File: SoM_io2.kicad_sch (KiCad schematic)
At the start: 1 part, among them J1 Hermaphroditic_Molex_203456-0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

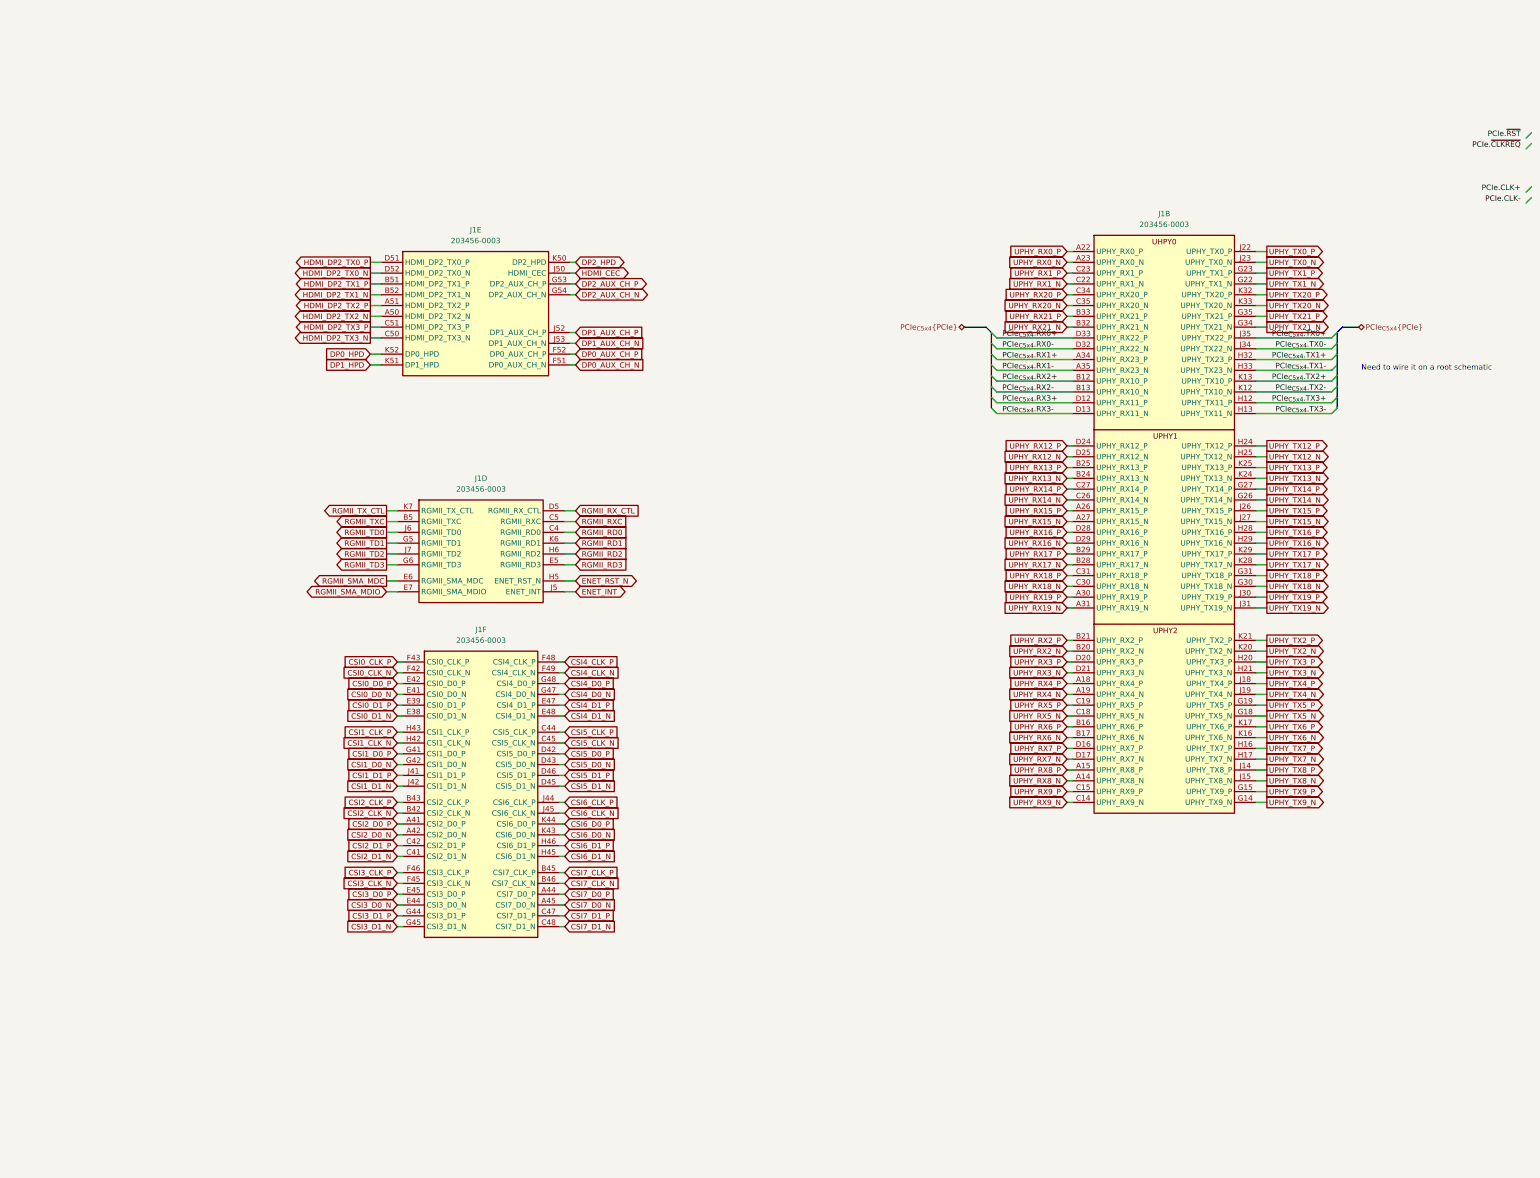
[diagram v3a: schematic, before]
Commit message: [#82048] Continue routing bus connections from M.2 key M to SoM
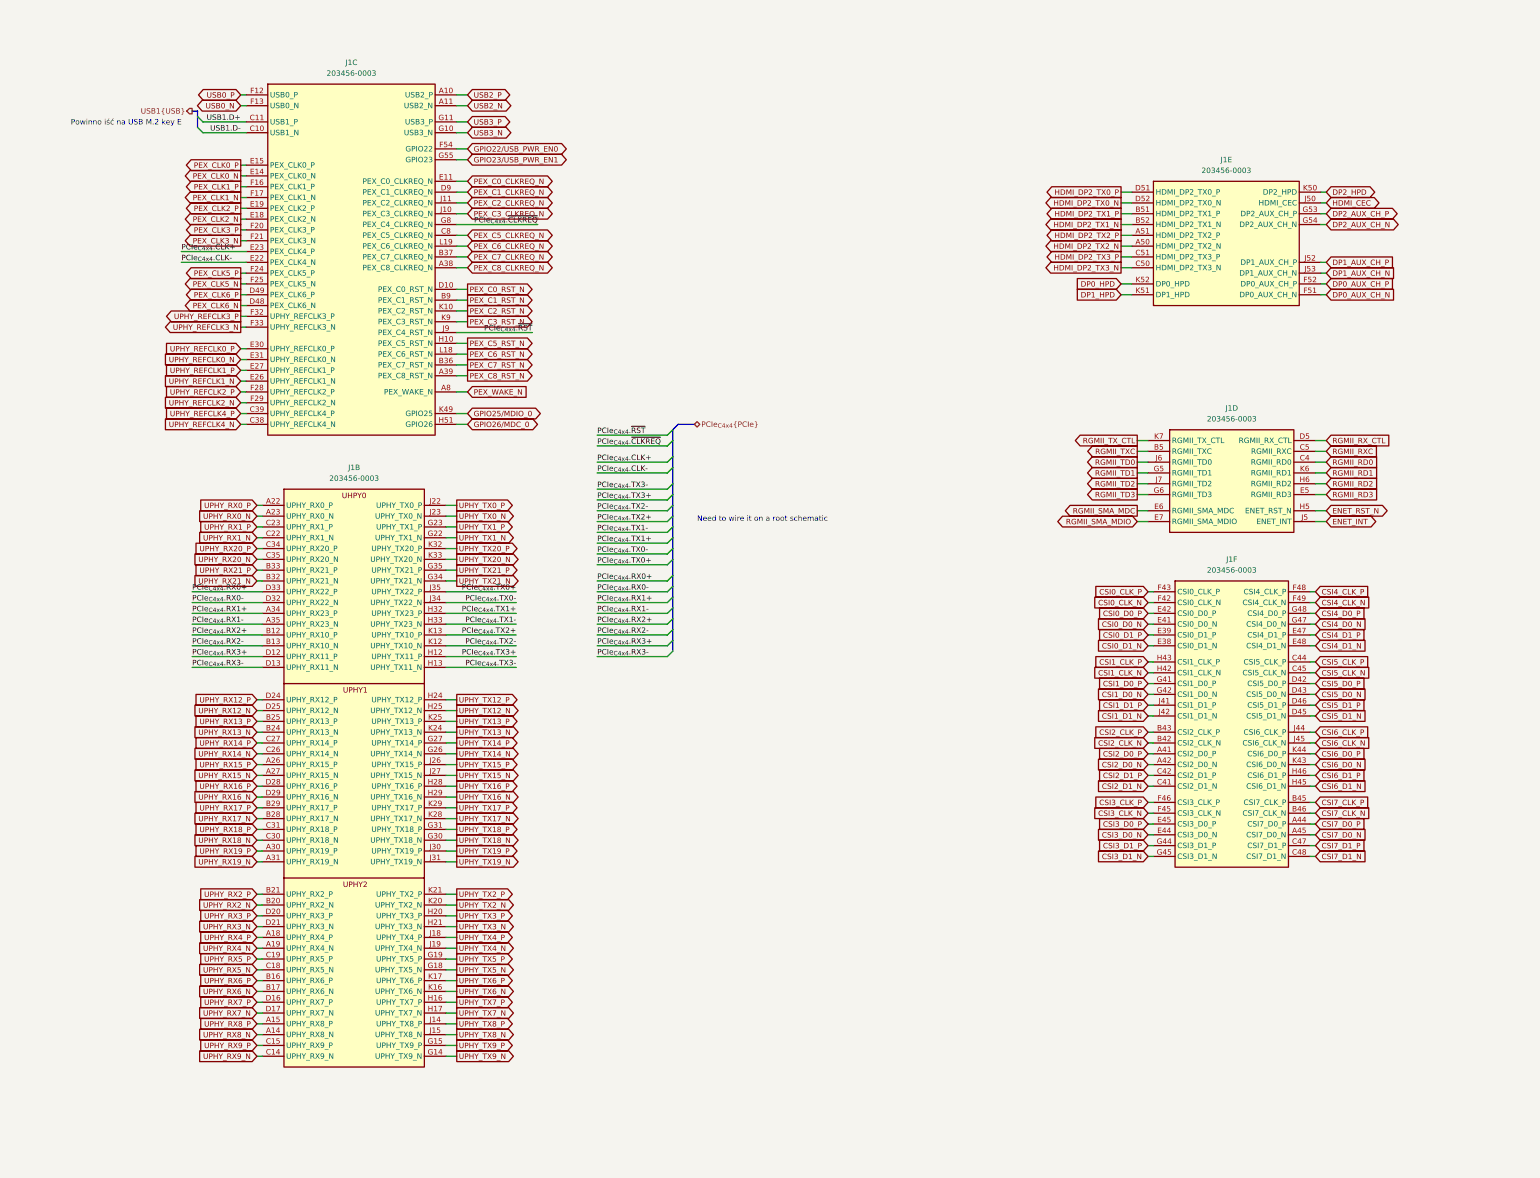
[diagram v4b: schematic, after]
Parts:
- added unit 3 of J1
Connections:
- net PCIe_{C5x4}.RX0+ renamed PCIe_{C4x4}.RX0+
- net PCIe_{C5x4}.RX0- renamed PCIe_{C4x4}.RX0-
- net PCIe_{C5x4}.RX1+ renamed PCIe_{C4x4}.RX1+
- net PCIe_{C5x4}.RX1- renamed PCIe_{C4x4}.RX1-
- net PCIe_{C5x4}.RX2+ renamed PCIe_{C4x4}.RX2+
- net PCIe_{C5x4}.RX2- renamed PCIe_{C4x4}.RX2-
- net PCIe_{C5x4}.RX3+ renamed PCIe_{C4x4}.RX3+
- net PCIe_{C5x4}.RX3- renamed PCIe_{C4x4}.RX3-
- net PCIe_{C5x4}.TX0+ renamed PCIe_{C4x4}.TX0+
- net PCIe_{C5x4}.TX0- renamed PCIe_{C4x4}.TX0-
- net PCIe_{C5x4}.TX1+ renamed PCIe_{C4x4}.TX1+
- net PCIe_{C5x4}.TX1- renamed PCIe_{C4x4}.TX1-
- net PCIe_{C5x4}.TX2+ renamed PCIe_{C4x4}.TX2+
- net PCIe_{C5x4}.TX2- renamed PCIe_{C4x4}.TX2-
- net PCIe_{C5x4}.TX3+ renamed PCIe_{C4x4}.TX3+
- net PCIe_{C5x4}.TX3- renamed PCIe_{C4x4}.TX3-
- new net GPIO22/USB_PWR_EN0: J1.F54 (GPIO22)
- new net GPIO23/USB_PWR_EN1: J1.G55 (GPIO23)
- new net GPIO25/MDIO_0: J1.K49 (GPIO25)
- new net GPIO26/MDC_0: J1.H51 (GPIO26)
- new net PCIe_{C4x4}.CLK+: J1.E23 (PEX_CLK4_P)
- new net PCIe_{C4x4}.CLK-: J1.E22 (PEX_CLK4_N)
- new net PCIe_{C4x4}.~{CLKREQ}: J1.G8 (PEX_C4_CLKREQ_N)
- new net PCIe_{C4x4}.~{RST}: J1.J9 (PEX_C4_RST_N)
- new net PEX_C0_CLKREQ_N: J1.E11 (PEX_C0_CLKREQ_N)
- new net PEX_C0_RST_N: J1.D10 (PEX_C0_RST_N)
- new net PEX_C1_CLKREQ_N: J1.D9 (PEX_C1_CLKREQ_N)
- new net PEX_C1_RST_N: J1.B9 (PEX_C1_RST_N)
- new net PEX_C2_CLKREQ_N: J1.J11 (PEX_C2_CLKREQ_N)
- new net PEX_C2_RST_N: J1.K10 (PEX_C2_RST_N)
- new net PEX_C3_CLKREQ_N: J1.J10 (PEX_C3_CLKREQ_N)
- new net PEX_C3_RST_N: J1.K9 (PEX_C3_RST_N)
- new net PEX_C5_CLKREQ_N: J1.C8 (PEX_C5_CLKREQ_N)
- new net PEX_C5_RST_N: J1.H10 (PEX_C5_RST_N)
- new net PEX_C6_CLKREQ_N: J1.L19 (PEX_C6_CLKREQ_N)
- new net PEX_C6_RST_N: J1.L18 (PEX_C6_RST_N)
- new net PEX_C7_CLKREQ_N: J1.B37 (PEX_C7_CLKREQ_N)
- new net PEX_C7_RST_N: J1.B36 (PEX_C7_RST_N)
- new net PEX_C8_CLKREQ_N: J1.A38 (PEX_C8_CLKREQ_N)
- new net PEX_C8_RST_N: J1.A39 (PEX_C8_RST_N)
- new net PEX_CLK0_N: J1.E14 (PEX_CLK0_N)
- new net PEX_CLK0_P: J1.E15 (PEX_CLK0_P)
- new net PEX_CLK1_N: J1.F17 (PEX_CLK1_N)
- new net PEX_CLK1_P: J1.F16 (PEX_CLK1_P)
- new net PEX_CLK2_N: J1.E18 (PEX_CLK2_N)
- new net PEX_CLK2_P: J1.E19 (PEX_CLK2_P)
- new net PEX_CLK3_N: J1.F21 (PEX_CLK3_N)
- new net PEX_CLK3_P: J1.F20 (PEX_CLK3_P)
- new net PEX_CLK5_N: J1.F25 (PEX_CLK5_N)
- new net PEX_CLK5_P: J1.F24 (PEX_CLK5_P)
- new net PEX_CLK6_N: J1.D48 (PEX_CLK6_N)
- new net PEX_CLK6_P: J1.D49 (PEX_CLK6_P)
- new net PEX_WAKE_N: J1.A8 (PEX_WAKE_N)
- new net UPHY_REFCLK0_N: J1.E31 (UPHY_REFCLK0_N)
- new net UPHY_REFCLK0_P: J1.E30 (UPHY_REFCLK0_P)
- new net UPHY_REFCLK1_N: J1.E26 (UPHY_REFCLK1_N)
- new net UPHY_REFCLK1_P: J1.E27 (UPHY_REFCLK1_P)
- new net UPHY_REFCLK2_N: J1.F29 (UPHY_REFCLK2_N)
- new net UPHY_REFCLK2_P: J1.F28 (UPHY_REFCLK2_P)
- new net UPHY_REFCLK3_N: J1.F33 (UPHY_REFCLK3_N)
- new net UPHY_REFCLK3_P: J1.F32 (UPHY_REFCLK3_P)
- new net UPHY_REFCLK4_N: J1.C38 (UPHY_REFCLK4_N)
- new net UPHY_REFCLK4_P: J1.C39 (UPHY_REFCLK4_P)
- new net USB0_N: J1.F13 (USB0_N)
- new net USB0_P: J1.F12 (USB0_P)
- new net USB1.D+: J1.C11 (USB1_P)
- new net USB1.D-: J1.C10 (USB1_N)
- new net USB2_N: J1.A11 (USB2_N)
- new net USB2_P: J1.A10 (USB2_P)
- new net USB3_N: J1.G10 (USB3_N)
- new net USB3_P: J1.G11 (USB3_P)
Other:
- note added: "Powinno iść na USB M.2 key E"
- moved on the sheet: J1B, J1D, J1E, J1F

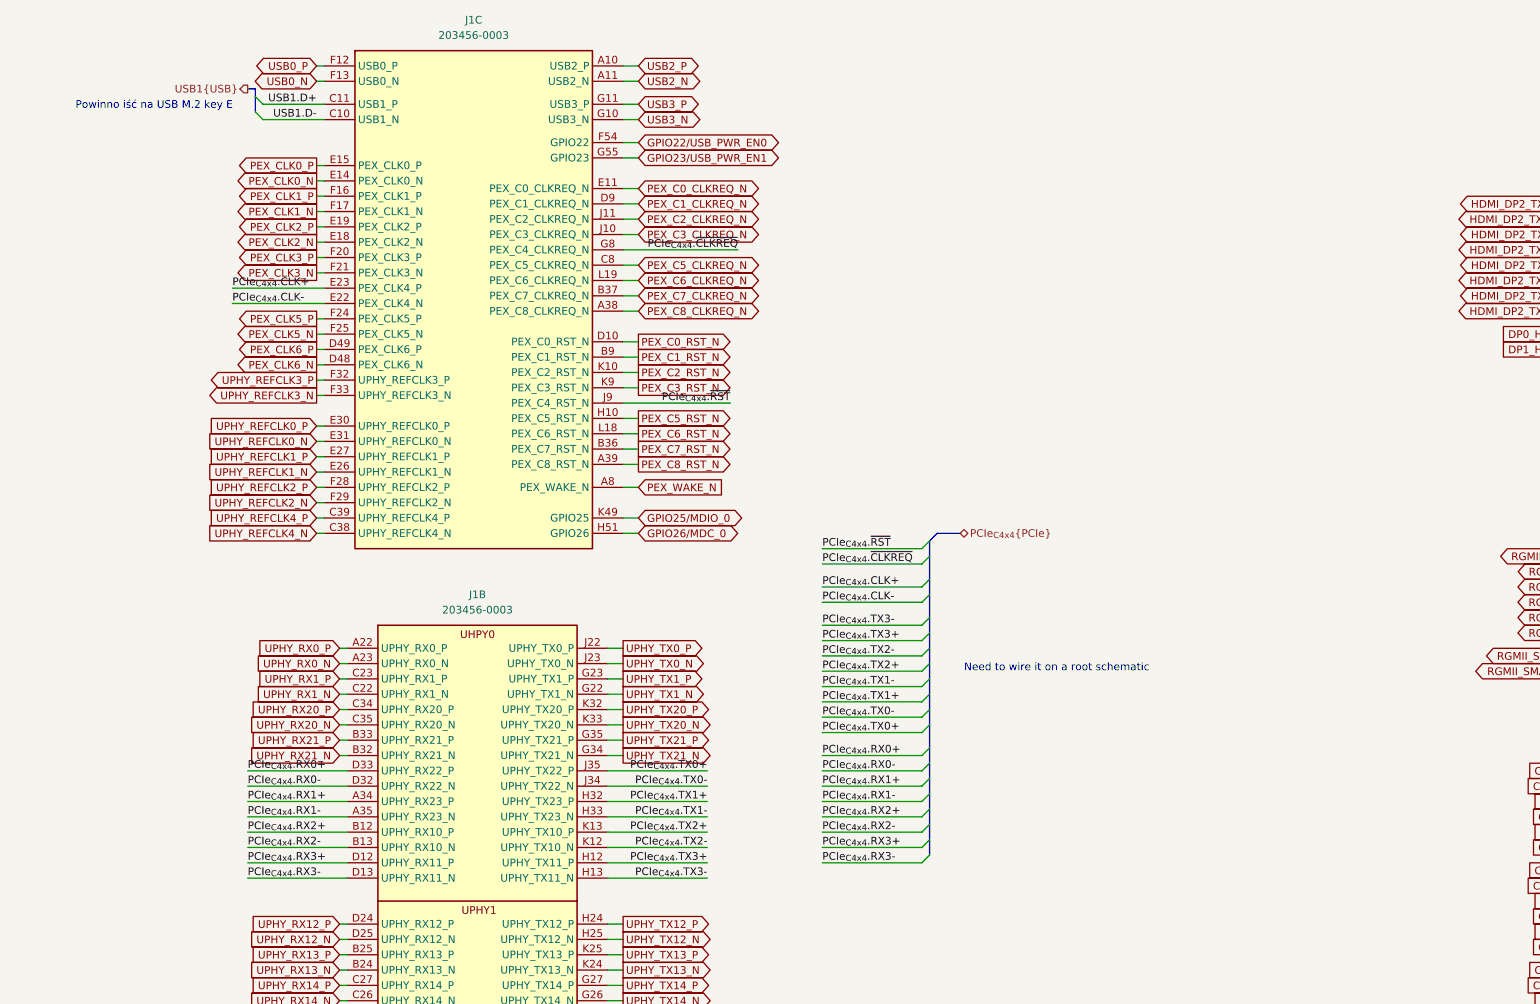
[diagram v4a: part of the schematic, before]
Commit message: [#82048] Route PCIe from M.2 key E to SoM
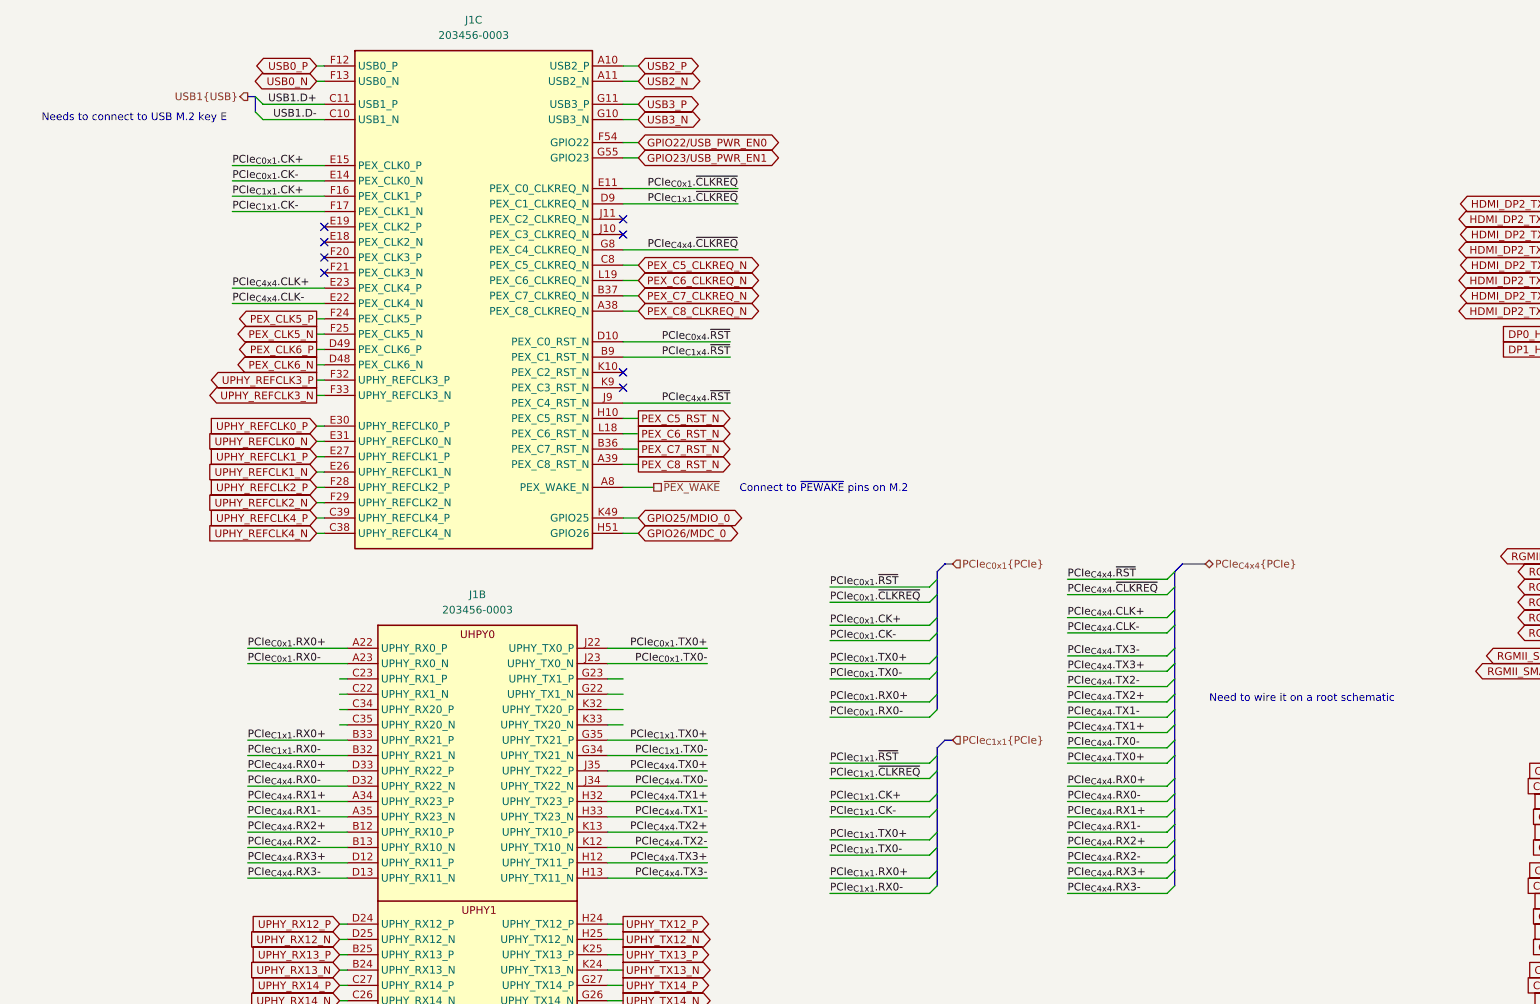
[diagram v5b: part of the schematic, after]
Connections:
- net PEX_C0_CLKREQ_N renamed PCIe_{C0x1}.~{CLKREQ}
- net PEX_C0_RST_N renamed PCIe_{C0x4}.~{RST}
- net PEX_C1_CLKREQ_N renamed PCIe_{C1x1}.~{CLKREQ}
- net PEX_C1_RST_N renamed PCIe_{C1x4}.~{RST}
- net PEX_C2_CLKREQ_N: no longer names the net of J1.J11 (PEX_C2_CLKREQ_N)
- net PEX_C2_RST_N: no longer names the net of J1.K10 (PEX_C2_RST_N)
- net PEX_C3_CLKREQ_N: no longer names the net of J1.J10 (PEX_C3_CLKREQ_N)
- net PEX_C3_RST_N: no longer names the net of J1.K9 (PEX_C3_RST_N)
- net PEX_CLK0_N renamed PCIe_{C0x1}.CK-
- net PEX_CLK0_P renamed PCIe_{C0x1}.CK+
- net PEX_CLK1_N renamed PCIe_{C1x1}.CK-
- net PEX_CLK1_P renamed PCIe_{C1x1}.CK+
- net PEX_CLK2_N: no longer names the net of J1.E18 (PEX_CLK2_N)
- net PEX_CLK2_P: no longer names the net of J1.E19 (PEX_CLK2_P)
- net PEX_CLK3_N: no longer names the net of J1.F21 (PEX_CLK3_N)
- net PEX_CLK3_P: no longer names the net of J1.F20 (PEX_CLK3_P)
- net PEX_WAKE_N renamed ~{PEX_WAKE}
- net UPHY_RX0_N renamed PCIe_{C0x1}.RX0-
- net UPHY_RX0_P renamed PCIe_{C0x1}.RX0+
- net UPHY_RX1_N: no longer names the net of J1.C22 (UPHY_RX1_N)
- net UPHY_RX1_P: no longer names the net of J1.C23 (UPHY_RX1_P)
- net UPHY_RX20_N: no longer names the net of J1.C35 (UPHY_RX20_N)
- net UPHY_RX20_P: no longer names the net of J1.C34 (UPHY_RX20_P)
- net UPHY_RX21_N renamed PCIe_{C1x1}.RX0-
- net UPHY_RX21_P renamed PCIe_{C1x1}.RX0+
- net UPHY_TX0_N renamed PCIe_{C0x1}.TX0-
- net UPHY_TX0_P renamed PCIe_{C0x1}.TX0+
- net UPHY_TX1_N: no longer names the net of J1.G22 (UPHY_TX1_N)
- net UPHY_TX1_P: no longer names the net of J1.G23 (UPHY_TX1_P)
- net UPHY_TX20_N: no longer names the net of J1.K33 (UPHY_TX20_N)
- net UPHY_TX20_P: no longer names the net of J1.K32 (UPHY_TX20_P)
- net UPHY_TX21_N renamed PCIe_{C1x1}.TX0-
- net UPHY_TX21_P renamed PCIe_{C1x1}.TX0+
- no-connect marks 0 -> 8
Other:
- note added: "Connect to ~{PEWAKE} pins on M.2"
- note added: "Needs to connect to USB M.2 key E"
- note removed: "Powinno iść na USB M.2 key E"
